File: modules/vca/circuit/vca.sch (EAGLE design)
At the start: 51 parts, among them IC1 LM324N, IC2 LM324N

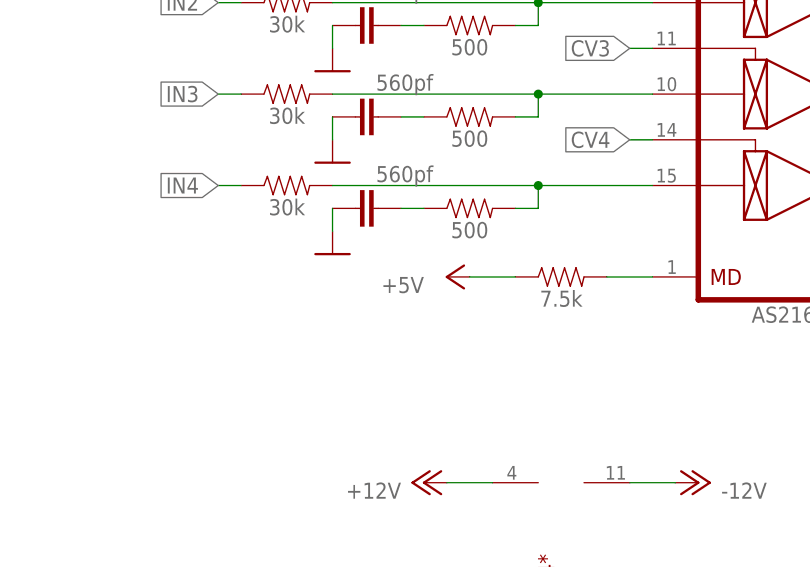
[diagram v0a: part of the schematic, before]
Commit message: VCA design
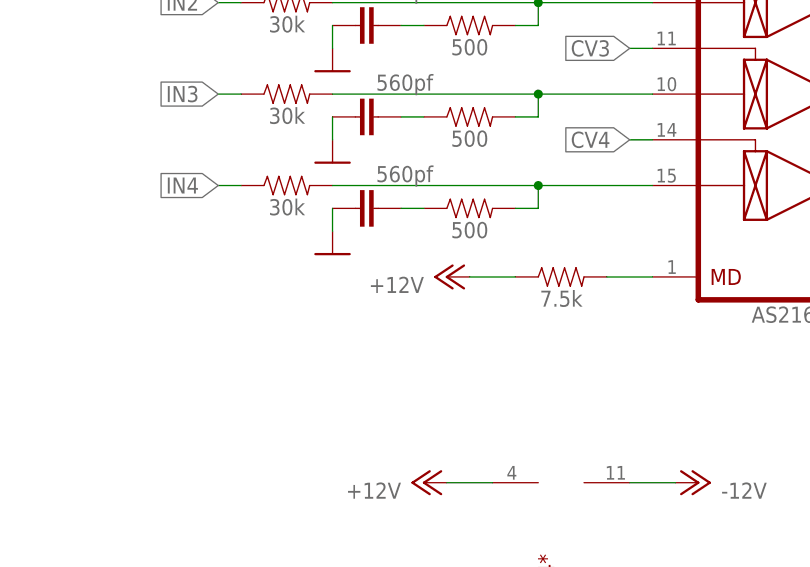
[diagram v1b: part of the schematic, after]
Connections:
- net +12V: now also R25.1
- net +5V: no longer R25.1
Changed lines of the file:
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@@
 <part name="P+7" library="supply1" library_urn="urn:adsk.eagle:library:371" deviceset="+12V" device=""/>
 <part name="R25" library="SparkFun-Resistors" deviceset="RESISTOR" device="AXIAL-0.3" value="7.5k"/>
-<part name="P+8" library="supply1" library_urn="urn:adsk.eagle:library:371" deviceset="+5V" device=""/>
 <part name="GND10" library="supply1" library_urn="urn:adsk.eagle:library:371" deviceset="GND" device=""/>
 <part name="P+9" library="supply1" library_urn="urn:adsk.eagle:library:371" deviceset="+12V" device=""/>
@@
 <part name="GND21" library="supply1" library_urn="urn:adsk.eagle:library:371" deviceset="GND" device=""/>
 <part name="GND22" library="supply1" library_urn="urn:adsk.eagle:library:371" deviceset="GND" device=""/>
+<part name="P+8" library="supply1" library_urn="urn:adsk.eagle:library:371" deviceset="+12V" device=""/>
 </parts>
 <sheets>
@@
 <attribute name="VALUE" x="172.72" y="161.036" size="1.778" layer="96" font="vector" align="top-center"/>
 </instance>
-<instance part="P+8" gate="1" x="160.02" y="162.56" smashed="yes" rot="R90">
-<attribute name="VALUE" x="157.48" y="162.56" size="1.778" layer="96" rot="R180"/>
-</instance>
 <instance part="AS2164" gate="*" x="172.72" y="127" smashed="yes" rot="R90">
 <attribute name="NAME" x="170.18" y="127" size="1.778" layer="94" rot="R270" align="bottom-center"/>
@@
 <instance part="GND21" gate="1" x="-99.06" y="142.24" smashed="yes"/>
 <instance part="GND22" gate="1" x="-99.06" y="124.46" smashed="yes"/>
+<instance part="P+8" gate="1" x="160.02" y="162.56" smashed="yes" rot="R90">
+<attribute name="VALUE" x="157.48" y="162.56" size="1.778" layer="96" rot="R180"/>
+</instance>
 </instances>
 <busses>
@@
 <pinref part="R22" gate="G$1" pin="2"/>
 <wire x1="-22.86" y1="114.3" x2="-20.32" y2="114.3" width="0.1524" layer="91"/>
-</segment>
-<segment>
-<pinref part="P+8" gate="1" pin="+5V"/>
-<pinref part="R25" gate="G$1" pin="1"/>
-<wire x1="162.56" y1="162.56" x2="167.64" y2="162.56" width="0.1524" layer="91"/>
 </segment>
 </net>
@@
 <wire x1="160.02" y1="139.7" x2="165.1" y2="139.7" width="0.1524" layer="91"/>
 </segment>
+<segment>
+<pinref part="R25" gate="G$1" pin="1"/>
+<wire x1="162.56" y1="162.56" x2="167.64" y2="162.56" width="0.1524" layer="91"/>
+<pinref part="P+8" gate="1" pin="+12V"/>
+</segment>
 </net>

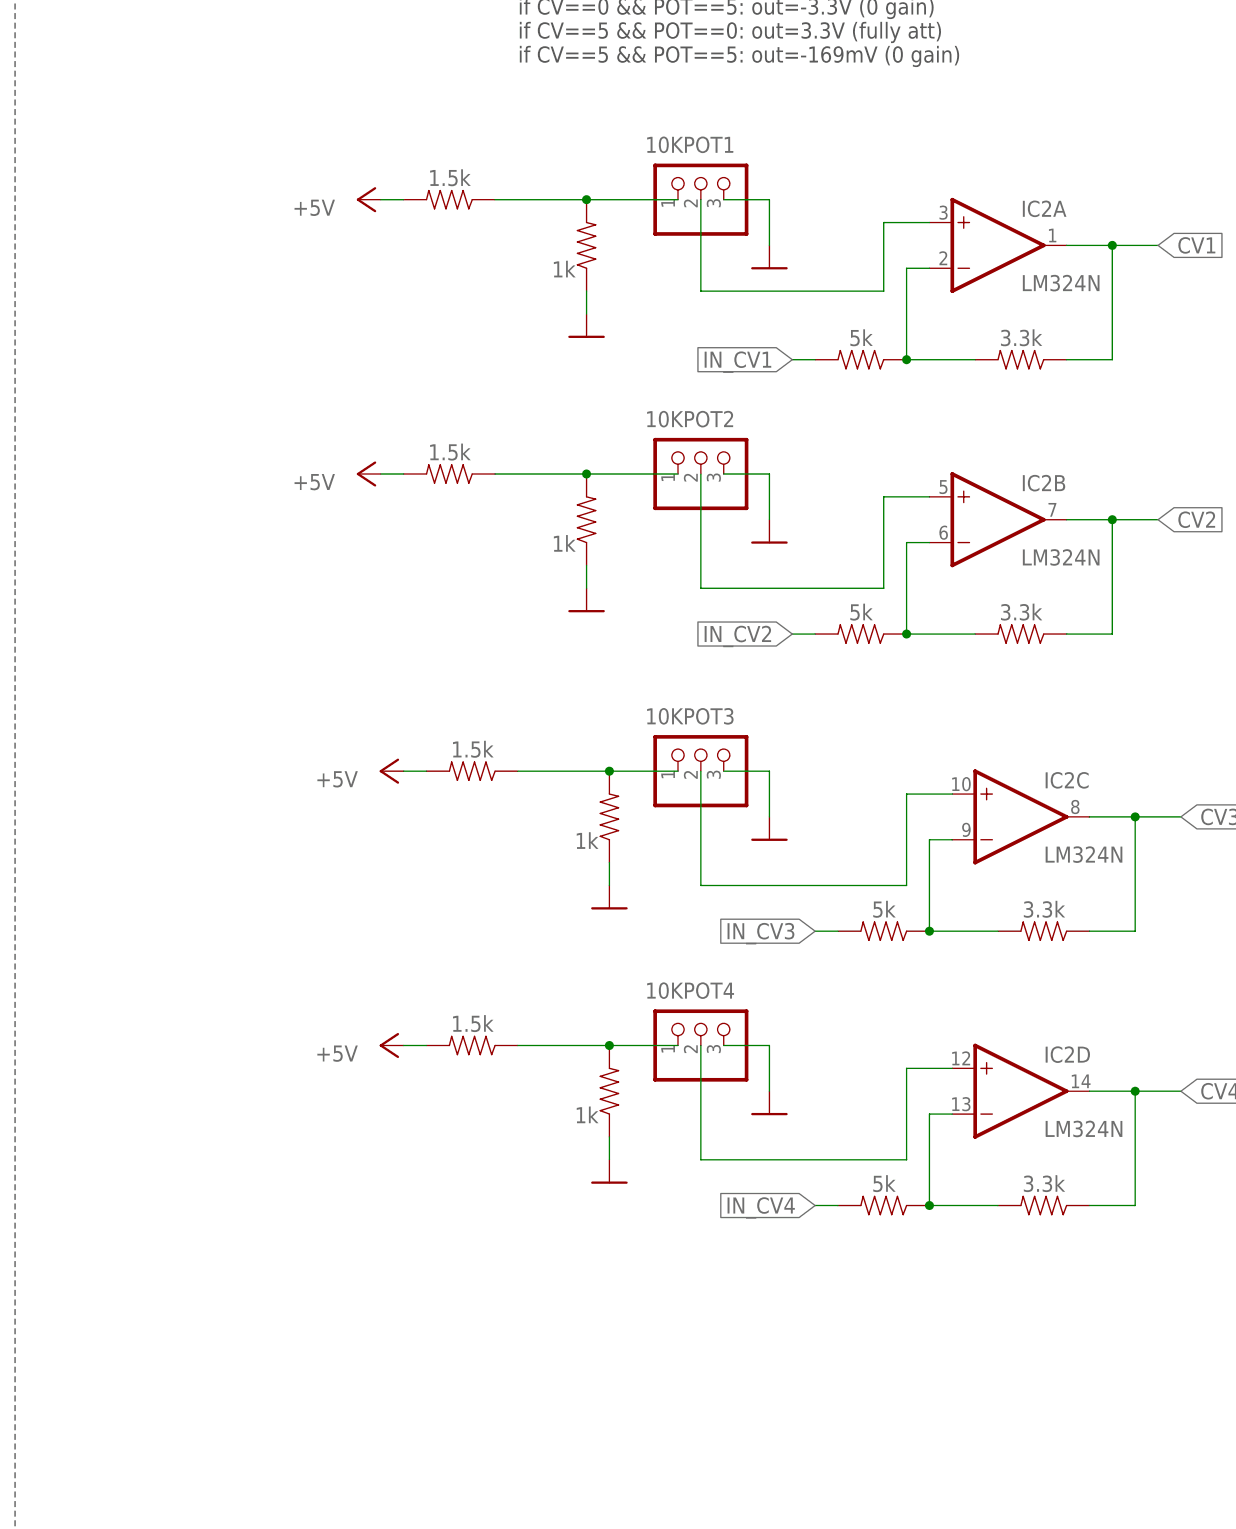
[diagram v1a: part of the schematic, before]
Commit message: Resistor changes for vca
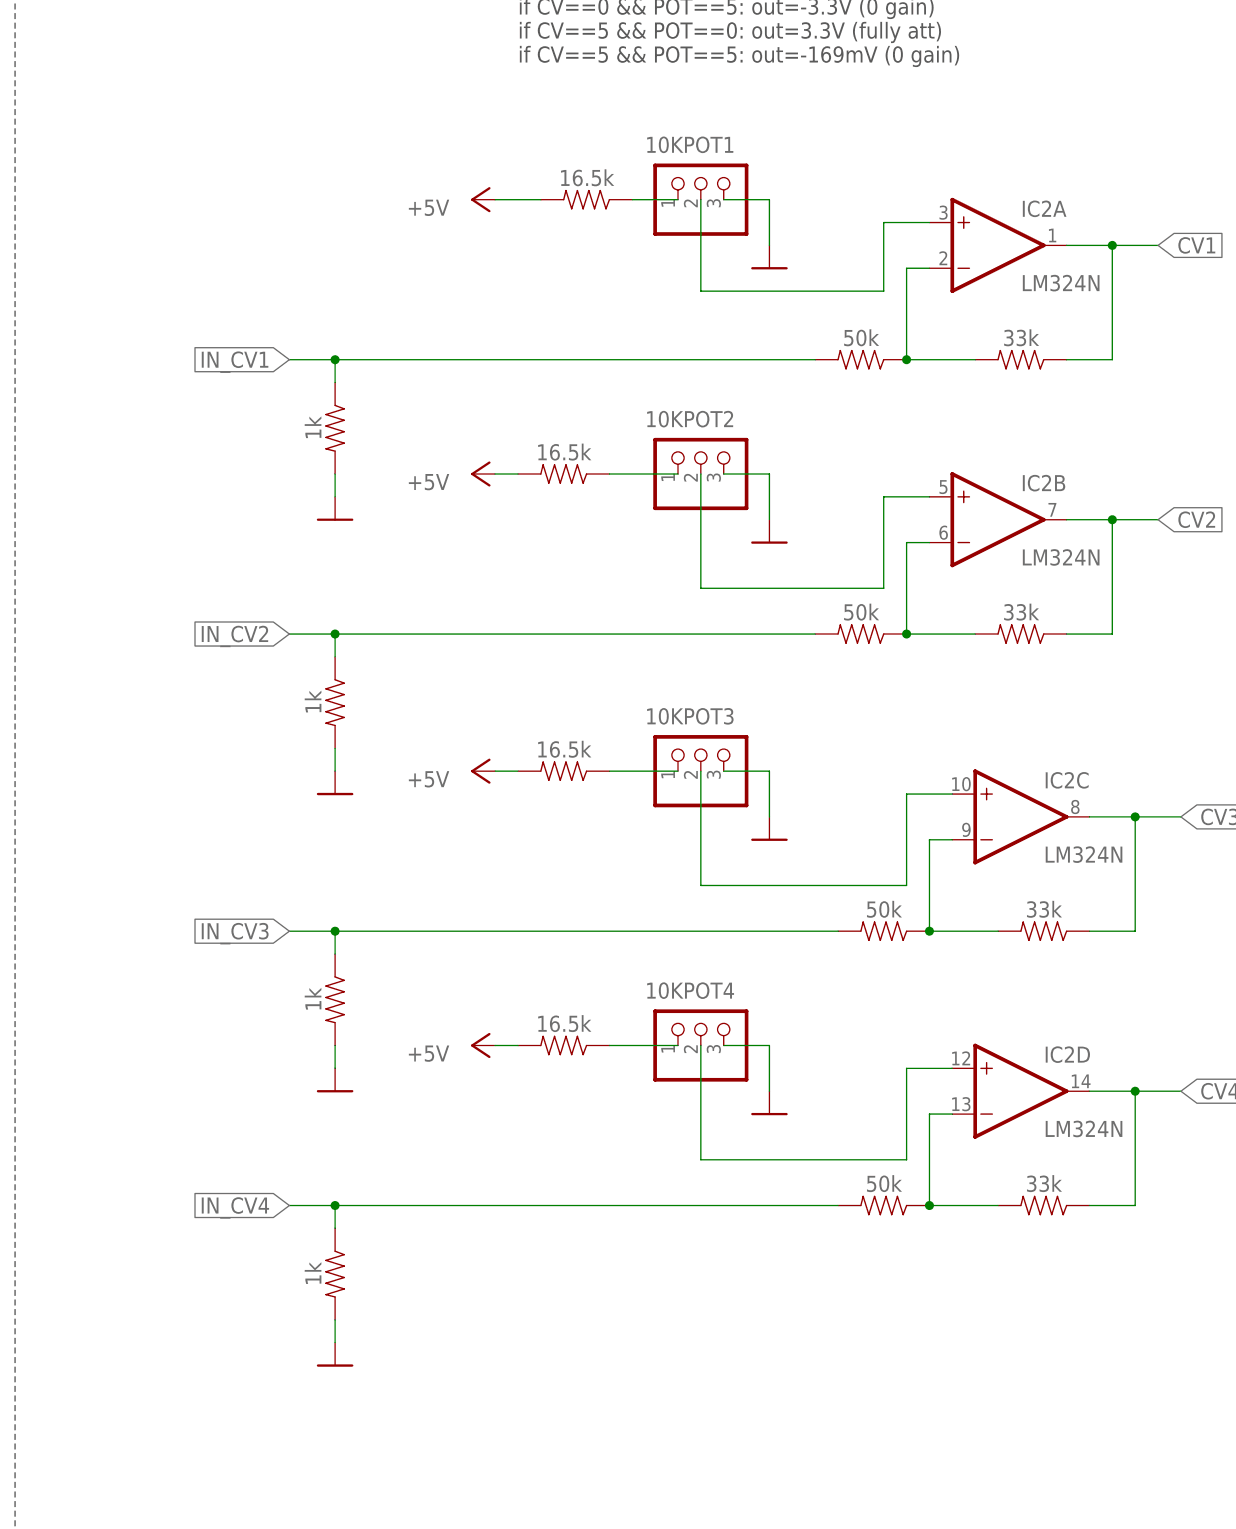
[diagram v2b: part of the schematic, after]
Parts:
- R10, R14, R18, R22: value 1.5k -> 16.5k
- R11, R15, R19, R23: value 5k -> 50k
- R12, R16, R20, R24: value 3.3k -> 33k
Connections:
- net GND: now also R13.2, R17.2, R21.2, R9.2; no longer R13.1, R17.1, R21.1, R9.1
- net IN_CV1: now also R9.1
- net IN_CV2: now also R13.1
- net IN_CV3: now also R17.1
- net IN_CV4: now also R21.1
- net N$10: no longer R9.2
- net N$13: no longer R13.2
- net N$16: no longer R17.2
- net N$19: no longer R21.2

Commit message: vca changes
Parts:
- removed 10KPOT1, 10KPOT2, 10KPOT3, 10KPOT4: (no value), pinhead:PINHD-1X3
- R11, R15, R19, R23: value 50k -> 47k
- R12, R16, R20, R24: value 33k -> 30k
- R13, R17, R21: value 1k -> 16.5k
- R14, R18, R22: value 16.5k -> 10k
- R9: value 1k -> 10k
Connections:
- removed net N$15: 10KPOT1.2, IC2A.+IN
- removed net N$16: 10KPOT1.1, R18.1
- removed net N$18: 10KPOT4.2, IC2D.+IN
- removed net N$19: 10KPOT4.1, R22.1
- net +5V: now also R10.1, R13.1, R17.1, R21.1; no longer R10.2, R14.2, R18.2, R22.2
- net GND: now also IC1A.+IN, IC1B.+IN, IC1C.+IN, IC1D.+IN, R14.1, R18.1, R22.1, R9.1; no longer 10KPOT1.3, 10KPOT2.3, 10KPOT3.3, 10KPOT4.3, IC1A.-IN, IC1B.-IN, IC1C.-IN, IC1D.-IN, R13.2, R17.2, R21.2, R9.2
- net IN_CV1: no longer R9.1
- net IN_CV2: no longer R13.1
- net IN_CV3: no longer R17.1
- net IN_CV4: no longer R21.1
- net N$10: now also IC2A.+IN, R10.2, R9.2; no longer 10KPOT3.1, R10.1
- net N$12: now also IC2C.+IN, R17.2, R18.2; no longer 10KPOT2.2, IC2B.+IN
- net N$13: now also IC2D.+IN, R21.2, R22.2; no longer 10KPOT2.1, R14.1
- net N$25: now also IC1D.-IN; no longer IC1D.+IN
- net N$31: now also IC1C.-IN; no longer IC1C.+IN
- net N$32: now also IC1B.-IN; no longer IC1B.+IN
- net N$33: now also IC1A.-IN; no longer IC1A.+IN
- net N$9: now also IC2B.+IN, R13.2, R14.2; no longer 10KPOT3.2, IC2C.+IN
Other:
- moved on the sheet: IC1A, IC1B, IC1C, IC1D

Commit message: modified VCA
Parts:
- R10, R13, R17, R21: value 16.5k -> 1k
- R11, R15, R19, R23: value 47k -> 100k
- R12, R16, R20, R24: value 30k -> 50k
- R14, R18, R22, R9: value 10k -> 500
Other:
- note removed: "if CV==0 && POT==0: out=-1.4mV (0 gain) if CV==0 && POT==5: out=-3.3V (0 gain) if CV==5 && POT==0: out=3.3V (fully att) if CV==5 && POT==5: out=-169mV (0 gain)"
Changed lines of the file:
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@@
 <?xml version="1.0" encoding="utf-8"?>
 <!DOCTYPE eagle SYSTEM "eagle.dtd">
-<eagle version="9.6.2">
+<eagle version="9.5.2">
 <drawing>
 <settings>
@@
 <part name="IC1" library="linear" library_urn="urn:adsk.eagle:library:262" deviceset="LM324" device="N" package3d_urn="urn:adsk.eagle:package:16407/2"/>
 <part name="IC2" library="linear" library_urn="urn:adsk.eagle:library:262" deviceset="LM324" device="N" package3d_urn="urn:adsk.eagle:package:16407/2"/>
-<part name="R11" library="SparkFun-Resistors" deviceset="RESISTOR" device="AXIAL-0.3" value="47k"/>
-<part name="R12" library="SparkFun-Resistors" deviceset="RESISTOR" device="AXIAL-0.3" value="30k"/>
-<part name="R15" library="SparkFun-Resistors" deviceset="RESISTOR" device="AXIAL-0.3" value="47k"/>
-<part name="R16" library="SparkFun-Resistors" deviceset="RESISTOR" device="AXIAL-0.3" value="30k"/>
+<part name="R11" library="SparkFun-Resistors" deviceset="RESISTOR" device="AXIAL-0.3" value="100k"/>
+<part name="R12" library="SparkFun-Resistors" deviceset="RESISTOR" device="AXIAL-0.3" value="50k"/>
+<part name="R15" library="SparkFun-Resistors" deviceset="RESISTOR" device="AXIAL-0.3" value="100k"/>
+<part name="R16" library="SparkFun-Resistors" deviceset="RESISTOR" device="AXIAL-0.3" value="50k"/>
 <part name="P+5" library="supply1" library_urn="urn:adsk.eagle:library:371" deviceset="+5V" device=""/>
-<part name="R19" library="SparkFun-Resistors" deviceset="RESISTOR" device="AXIAL-0.3" value="47k"/>
-<part name="R20" library="SparkFun-Resistors" deviceset="RESISTOR" device="AXIAL-0.3" value="30k"/>
-<part name="R23" library="SparkFun-Resistors" deviceset="RESISTOR" device="AXIAL-0.3" value="47k"/>
-<part name="R24" library="SparkFun-Resistors" deviceset="RESISTOR" device="AXIAL-0.3" value="30k"/>
+<part name="R19" library="SparkFun-Resistors" deviceset="RESISTOR" device="AXIAL-0.3" value="100k"/>
+<part name="R20" library="SparkFun-Resistors" deviceset="RESISTOR" device="AXIAL-0.3" value="50k"/>
+<part name="R23" library="SparkFun-Resistors" deviceset="RESISTOR" device="AXIAL-0.3" value="100k"/>
+<part name="R24" library="SparkFun-Resistors" deviceset="RESISTOR" device="AXIAL-0.3" value="50k"/>
 <part name="P-2" library="supply1" library_urn="urn:adsk.eagle:library:371" deviceset="-12V" device=""/>
 <part name="P+7" library="supply1" library_urn="urn:adsk.eagle:library:371" deviceset="+12V" device=""/>
@@
 <part name="GND22" library="supply1" library_urn="urn:adsk.eagle:library:371" deviceset="GND" device=""/>
 <part name="P+8" library="supply1" library_urn="urn:adsk.eagle:library:371" deviceset="+12V" device=""/>
-<part name="R10" library="SparkFun-Resistors" deviceset="RESISTOR" device="AXIAL-0.3" value="16.5k"/>
-<part name="R9" library="SparkFun-Resistors" deviceset="RESISTOR" device="AXIAL-0.3" value="10k"/>
+<part name="R10" library="SparkFun-Resistors" deviceset="RESISTOR" device="AXIAL-0.3" value="1k"/>
+<part name="R9" library="SparkFun-Resistors" deviceset="RESISTOR" device="AXIAL-0.3" value="500"/>
 <part name="GND6" library="supply1" library_urn="urn:adsk.eagle:library:371" deviceset="GND" device=""/>
 <part name="P+3" library="supply1" library_urn="urn:adsk.eagle:library:371" deviceset="+5V" device=""/>
-<part name="R13" library="SparkFun-Resistors" deviceset="RESISTOR" device="AXIAL-0.3" value="16.5k"/>
-<part name="R14" library="SparkFun-Resistors" deviceset="RESISTOR" device="AXIAL-0.3" value="10k"/>
+<part name="R13" library="SparkFun-Resistors" deviceset="RESISTOR" device="AXIAL-0.3" value="1k"/>
+<part name="R14" library="SparkFun-Resistors" deviceset="RESISTOR" device="AXIAL-0.3" value="500"/>
 <part name="GND7" library="supply1" library_urn="urn:adsk.eagle:library:371" deviceset="GND" device=""/>
 <part name="P+4" library="supply1" library_urn="urn:adsk.eagle:library:371" deviceset="+5V" device=""/>
-<part name="R17" library="SparkFun-Resistors" deviceset="RESISTOR" device="AXIAL-0.3" value="16.5k"/>
-<part name="R18" library="SparkFun-Resistors" deviceset="RESISTOR" device="AXIAL-0.3" value="10k"/>
+<part name="R17" library="SparkFun-Resistors" deviceset="RESISTOR" device="AXIAL-0.3" value="1k"/>
+<part name="R18" library="SparkFun-Resistors" deviceset="RESISTOR" device="AXIAL-0.3" value="500"/>
 <part name="GND8" library="supply1" library_urn="urn:adsk.eagle:library:371" deviceset="GND" device=""/>
 <part name="P+6" library="supply1" library_urn="urn:adsk.eagle:library:371" deviceset="+5V" device=""/>
-<part name="R21" library="SparkFun-Resistors" deviceset="RESISTOR" device="AXIAL-0.3" value="16.5k"/>
-<part name="R22" library="SparkFun-Resistors" deviceset="RESISTOR" device="AXIAL-0.3" value="10k"/>
+<part name="R21" library="SparkFun-Resistors" deviceset="RESISTOR" device="AXIAL-0.3" value="1k"/>
+<part name="R22" library="SparkFun-Resistors" deviceset="RESISTOR" device="AXIAL-0.3" value="500"/>
 <part name="GND9" library="supply1" library_urn="urn:adsk.eagle:library:371" deviceset="GND" device=""/>
 </parts>
@@
 <sheet>
 <plain>
-<text x="-10.16" y="223.52" size="1.778" layer="97">if CV==0 &amp;&amp; POT==0: out=-1.4mV (0 gain)
-if CV==0 &amp;&amp; POT==5: out=-3.3V (0 gain)
-if CV==5 &amp;&amp; POT==0: out=3.3V (fully att)
-if CV==5 &amp;&amp; POT==5: out=-169mV (0 gain)
-</text>
 <wire x1="-66.04" y1="284.48" x2="-66.04" y2="40.64" width="0.1524" layer="97" style="shortdash"/>
 <wire x1="104.14" y1="284.48" x2="104.14" y2="40.64" width="0.1524" layer="97" style="shortdash"/>
@@
 </drawing>
 <compatibility>
-<note version="6.3" minversion="6.2.2" severity="warning">
-Since Version 6.2.2 text objects can contain more than one line,
-which will not be processed correctly with this version.
-</note>
 <note version="8.2" severity="warning">
 Since Version 8.2, EAGLE supports online libraries. The ids
